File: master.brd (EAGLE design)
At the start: 27.3 x 34.3 mm, 9 parts

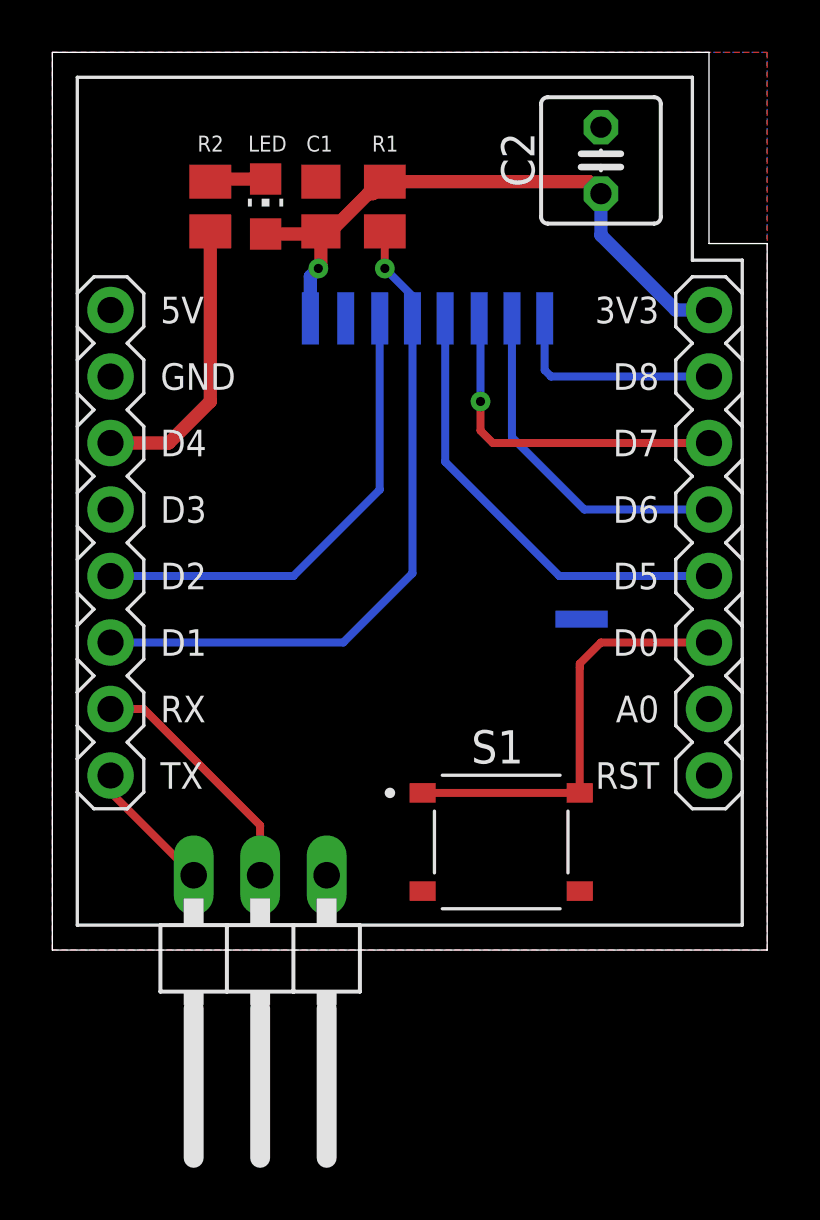
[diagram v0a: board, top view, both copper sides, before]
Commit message: poprawione polaczenia, usunieta masa pod antena,
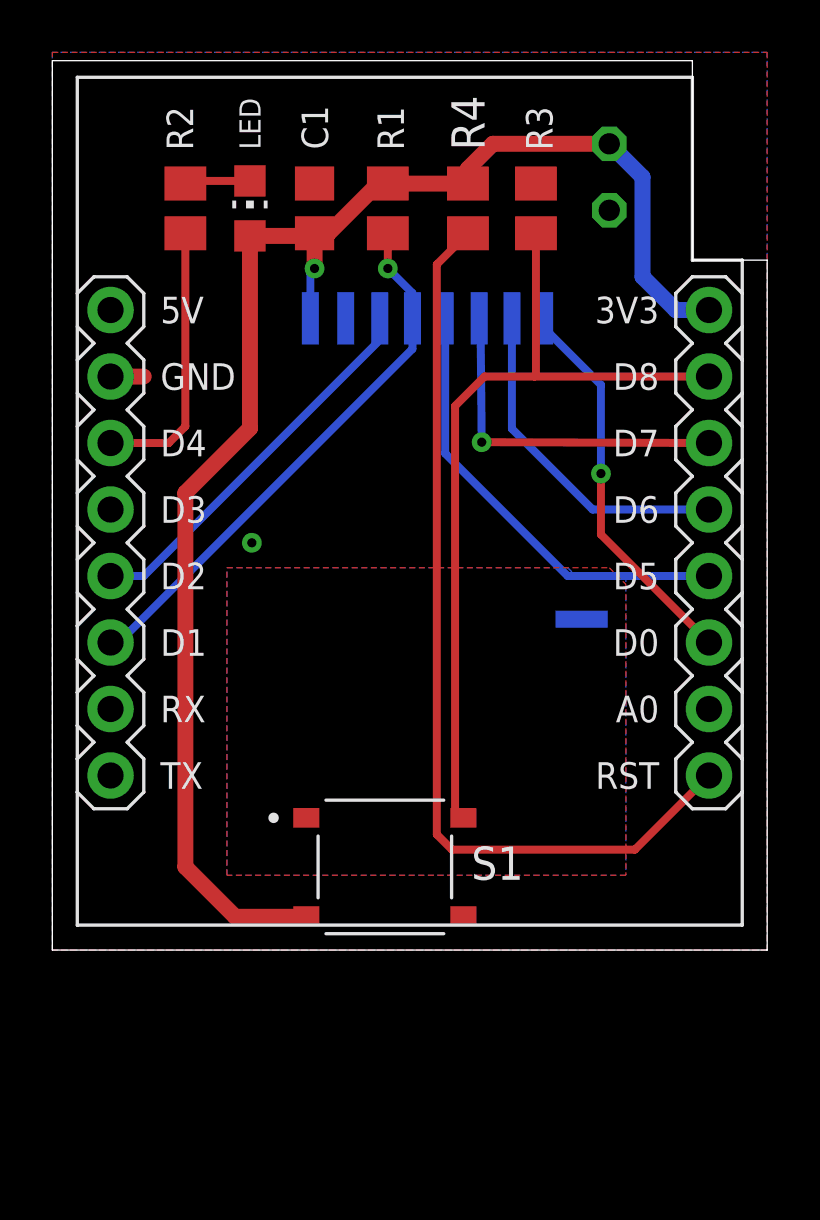
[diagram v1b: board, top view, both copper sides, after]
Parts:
- removed JP2: (no value), pinhead:1X03/90
- added R3: 47k, rcl:M0805
- added R4: 100k, rcl:M0805
- moved S1 4.55 mm to (12.7, 3.17)
- moved R2 0.96 mm to (5.08, 28.3)
- moved C2 0.71 mm to (21.3, 29.5), flipped to the bottom, turned to 270 degrees
- moved LED 0.60 mm to (7.55, 28.3)
- moved C1 0.25 mm to (10.0, 28.3)
- moved R1 0.14 mm to (12.8, 28.3)
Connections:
- removed net RX: JP2.2, U$2.JP2.2
- removed net TX: JP2.3, U$2.JP2.1
- new net RST: R4.2, U$2.JP1.1
- net +3V3: now also R4.1, S1.C, S1.D
- net BUTTON: now also R3.1, U$2.JP1.7; no longer U$2.JP1.3
- net GND: now also R3.2; no longer JP2.1, S1.C, S1.D
- net INTERRUPT: now also U$2.JP1.3; no longer U$2.JP1.7
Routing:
- net RST: track 0.00 -> 35.3 mm
- net +3V3: track 24.8 -> 58.1 mm
- net BUTTON: track 16.2 -> 31.7 mm
- net RX: track 9.46 -> 0.00 mm
- net INTERRUPT: track 8.36 -> 15.0 mm, vias 0 -> 1
- net CSN: track 26.1 -> 21.0 mm
- net TX: track 5.13 -> 0.00 mm
- net CE: track 18.2 -> 14.8 mm
- net GND: track 0.00 -> 1.27 mm, vias 0 -> 1
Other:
- board size 27.3 x 34.3 mm -> 27.3 x 34 mm
- board text removed: "C1"
- board text removed: "C2"
- board text removed: "LED"
- board text removed: "R1"
- board text removed: "R2"
- board text removed: "S1"

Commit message: dodanei warstwy opisowej do panelizacji
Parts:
- moved S1 7.30 mm to (20.0, 3.17)
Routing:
- net +3V3: track 58.1 -> 71.4 mm
- net BUTTON: track 31.7 -> 39.2 mm
- net RST: track 35.3 -> 36.0 mm
- net MOSI: track 13.4 -> 13.2 mm, vias 1 -> 0
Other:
- board text added: "C1"
- board text added: "C2"
- board text added: "LED"
- board text added: "R1"
- board text added: "R2"
- board text added: "R3"
- board text added: "R4"
- board text added: "S1"
- board text added: "by Dominik Nowocień v1.1"
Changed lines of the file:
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@@
 <drawing>
 <settings>
-<setting alwaysvectorfont="no"/>
+<setting alwaysvectorfont="yes"/>
 <setting verticaltext="up"/>
 </settings>
@@
 <layer number="97" name="Info" color="7" fill="1" visible="no" active="no"/>
 <layer number="98" name="Guide" color="6" fill="1" visible="no" active="no"/>
-<layer number="101" name="Hidden" color="15" fill="1" visible="yes" active="yes"/>
-<layer number="102" name="Changes" color="12" fill="1" visible="yes" active="yes"/>
-<layer number="125" name="_tNames" color="7" fill="1" visible="no" active="yes"/>
+<layer number="100" name="opis_dol" color="7" fill="1" visible="yes" active="yes"/>
+<layer number="101" name="opis_gora" color="7" fill="1" visible="no" active="yes"/>
+<layer number="125" name="_tNames" color="14" fill="1" visible="yes" active="yes"/>
+<layer number="126" name="_bNames" color="5" fill="1" visible="yes" active="yes"/>
 </layers>
 <board>
@@
 <wire x1="0" y1="0" x2="27.305" y2="0" width="0" layer="20"/>
 <text x="6.6675" y="20.6375" size="1.4224" layer="22" rot="MR270">NRF24L01+</text>
+<text x="13.75" y="3.135" size="1.27" layer="100" rot="SR180" align="center">by Dominik Nowocień v1.1</text>
+<text x="10.534115625" y="30.582540625" size="1.016" layer="125" rot="R90">C1</text>
+<text x="18.415" y="30.226" size="1.27" layer="126" ratio="10" rot="MR270">C2</text>
+<text x="7.9558125" y="30.582540625" size="0.8128" layer="125" rot="R90">LED</text>
+<text x="13.42991875" y="30.551653125" size="1.016" layer="125" rot="R90">R1</text>
+<text x="5.377509375" y="30.551653125" size="1.016" layer="125" rot="R90">R2</text>
+<text x="19.10745625" y="30.551653125" size="1.016" layer="125" rot="R90">R3</text>
+<text x="16.51" y="30.551653125" size="1.27" layer="125" rot="R90">R4</text>
+<text x="23.305009375" y="2.68249375" size="1.27" layer="125">S1</text>
 </plain>
 <attributes>
@@
 <attribute name="VALUE" x="7.62" y="27.05915" size="1.27" layer="27" rot="R90"/>
 </element>
-<element name="S1" library="Modules" package="SW_TS-1187A-B-A-B" package3d_urn="urn:adsk.eagle:package:24754950/2" value="TS-1187A-B-A-B" x="12.7" y="3.175" smashed="yes">
-<attribute name="NAME" x="16.0025" y="2.6825" size="1.27" layer="25"/>
+<element name="S1" library="Modules" package="SW_TS-1187A-B-A-B" package3d_urn="urn:adsk.eagle:package:24754950/2" value="TS-1187A-B-A-B" x="20.0025" y="3.175" smashed="yes">
+<attribute name="NAME" x="23.305" y="2.6825" size="1.27" layer="25"/>
 </element>
 <element name="R3" library="rcl" library_urn="urn:adsk.eagle:library:334" package="M0805" package3d_urn="urn:adsk.eagle:package:23556/2" value="47k" x="18.47245" y="28.32915" smashed="yes" rot="R90">
@@
 <wire x1="5.08" y1="17.4625" x2="5.08" y2="3.175" width="0.6096" layer="1"/>
 <wire x1="5.08" y1="3.175" x2="6.985" y2="1.27" width="0.6096" layer="1"/>
-<wire x1="6.985" y1="1.27" x2="9.67" y2="1.27" width="0.6096" layer="1"/>
-<wire x1="9.67" y1="1.27" x2="9.7" y2="1.3" width="0.3048" layer="1"/>
-<wire x1="10.014875" y1="26.035" x2="9.855" y2="25.875125" width="0.3048" layer="16"/>
-<wire x1="9.855" y1="25.875125" x2="9.855" y2="24.13" width="0.3048" layer="16"/>
-<wire x1="9.7" y1="1.3" x2="15.7" y2="1.3" width="0" layer="19" extent="1-1"/>
+<wire x1="16.9725" y1="1.27" x2="6.985" y2="1.27" width="0.6096" layer="1"/>
+<wire x1="9.855" y1="24.13" x2="9.855" y2="25.875125" width="0.5" layer="16"/>
+<wire x1="9.855" y1="25.875125" x2="10.014875" y2="26.035" width="0.5" layer="16"/>
+<wire x1="17.0025" y1="1.3" x2="23.0025" y2="1.3" width="0.5" layer="1"/>
+<wire x1="17.0025" y1="1.3" x2="16.9725" y2="1.27" width="0.5" layer="1"/>
 </signal>
 <signal name="GND" class="1">
@@
 <signal name="MOSI">
 <contactref element="U$2" pad="JP1.6"/>
-<via x="16.4" y="19.4" extent="1-16" drill="0.35"/>
-<wire x1="16.4" y1="19.4" x2="16.3546" y2="24.0804" width="0.3048" layer="16"/>
-<wire x1="16.3546" y1="24.0804" x2="16.305" y2="24.13" width="0.3048" layer="16"/>
+<wire x1="16.305" y1="24.13" x2="16.41465" y2="24.23965" width="0.3048" layer="16"/>
 <contactref element="NRF24" pad="6"/>
-<wire x1="25.0825" y1="19.3675" x2="16.4" y2="19.4" width="0.3048" layer="1"/>
+<wire x1="16.305" y1="24.13" x2="16.305" y2="25.195" width="0.5" layer="16"/>
+<wire x1="16.305" y1="25.195" x2="16.8275" y2="25.7175" width="0.5" layer="16"/>
+<wire x1="16.8275" y1="25.7175" x2="19.3675" y2="25.7175" width="0.5" layer="16"/>
+<wire x1="23.495" y1="21.59" x2="23.495" y2="20.955" width="0.5" layer="16"/>
+<wire x1="23.495" y1="20.955" x2="25.0825" y2="19.3675" width="0.5" layer="16"/>
+<wire x1="19.3675" y1="25.7175" x2="23.495" y2="21.59" width="0.5" layer="16"/>
 </signal>
 <signal name="CSN">
@@
 <contactref element="U$2" pad="JP1.7"/>
 <wire x1="15.3825" y1="20.78" x2="15.3825" y2="5.05" width="0.3048" layer="1"/>
-<wire x1="15.7" y1="5.05" x2="15.3825" y2="5.05" width="0.3048" layer="1"/>
+<wire x1="23.0025" y1="5.05" x2="17.145" y2="5.05" width="0.3048" layer="1"/>
+<wire x1="17.145" y1="5.05" x2="15.3825" y2="5.05" width="0.3048" layer="1"/>
 <wire x1="25.0825" y1="21.9075" x2="18.415" y2="21.9075" width="0.3048" layer="1"/>
 <contactref element="S1" pad="B"/>
@@
 <wire x1="15.3825" y1="20.78" x2="16.51" y2="21.9075" width="0.3048" layer="1"/>
 <wire x1="16.51" y1="21.9075" x2="18.415" y2="21.9075" width="0.3048" layer="1"/>
-<wire x1="9.7" y1="5.05" x2="15.7" y2="5.05" width="0" layer="19" extent="1-1"/>
+<wire x1="17.0025" y1="5.05" x2="17.145" y2="5.05" width="0.1524" layer="1"/>
 </signal>
 <signal name="INTERRUPT">
@@
 <wire x1="14.6852" y1="26.1893625" x2="14.6852" y2="4.415" width="0.3048" layer="1"/>
 <wire x1="15.2651" y1="3.8351" x2="14.6852" y2="4.415" width="0.3048" layer="1"/>
-<wire x1="25.0825" y1="6.6675" x2="22.2501" y2="3.8351" width="0.3048" layer="1"/>
-<wire x1="22.2501" y1="3.8351" x2="15.2651" y2="3.8351" width="0.3048" layer="1"/>
+<wire x1="25.0825" y1="6.6675" x2="25.0825" y2="5.3975" width="0.3048" layer="1"/>
+<wire x1="25.0825" y1="5.3975" x2="23.5201" y2="3.8351" width="0.3048" layer="1"/>
+<wire x1="23.5201" y1="3.8351" x2="15.2651" y2="3.8351" width="0.3048" layer="1"/>
 </signal>
 </signals>

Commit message: drobne poprawki
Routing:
- net RST: track 36.0 -> 50.3 mm
- net BUTTON: track 39.2 -> 27.1 mm
- net SCK: track 17.2 -> 14.9 mm
- net MISO: track 13.0 -> 11.5 mm
- net GND: vias 1 -> 2
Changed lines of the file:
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@@
 </layers>
 <board>
-<fusionsync huburn="a.YnVzaW5lc3M6c3R1ZGVudDQ4Njkw" projecturn="a.YnVzaW5lc3M6c3R1ZGVudDQ4NjkwI0QyMDIwMTEwOTM1MTQzNTM4MQ" f3durn="urn:adsk.wipprod:dm.lineage:U4Mw_bNETOOnVXnWI0y87Q" pcbguid="" lastpulledtime="" lastsyncedchangeguid="" latestrevisionid="d24e285d-8679-4091-b8af-5643a4074593" lastsyncedrevisionid="d24e285d-8679-4091-b8af-5643a4074593" lastboardhashguid="a275b44c-f568-7217-ba50-b1bd45fb6022" lastpushedtime="2020-12-21T23:49:28Z" linktopcb3d="true"/>
+<fusionsync huburn="a.YnVzaW5lc3M6c3R1ZGVudDQ4Njkw" projecturn="a.YnVzaW5lc3M6c3R1ZGVudDQ4NjkwI0QyMDIwMTEwOTM1MTQzNTM4MQ" f3durn="urn:adsk.wipprod:dm.lineage:U4Mw_bNETOOnVXnWI0y87Q" pcbguid="" lastpulledtime="" lastsyncedchangeguid="" latestrevisionid="adf31d11-2971-490c-9e2a-feead3d7f8aa" lastsyncedrevisionid="adf31d11-2971-490c-9e2a-feead3d7f8aa" lastboardhashguid="4a1d11f1-682a-e53e-9940-e431d41f0d06" lastpushedtime="2020-12-31T12:38:42Z" linktopcb3d="true"/>
 <plain>
 <wire x1="27.305" y1="26.3525" x2="24.4475" y2="26.3525" width="0" layer="20"/>
@@
 <contactref element="LED" pad="A"/>
 <contactref element="U$2" pad="JP1.8"/>
-<wire x1="10.014875" y1="27.37915" x2="10.014875" y2="26.035" width="0.6096" layer="1"/>
-<via x="10.014875" y="26.035" extent="1-16" drill="0.35"/>
+<wire x1="10.014875" y1="27.37915" x2="10.014875" y2="26" width="0.6096" layer="1"/>
+<via x="10.014875" y="26" extent="1-16" drill="0.35"/>
 <wire x1="9.88615" y1="27.3508" x2="9.8145" y2="27.27915" width="0.6096" layer="1"/>
 <wire x1="9.8145" y1="27.27915" x2="7.5474375" y2="27.27915" width="0.6096" layer="1"/>
@@
 <wire x1="16.9725" y1="1.27" x2="6.985" y2="1.27" width="0.6096" layer="1"/>
 <wire x1="9.855" y1="24.13" x2="9.855" y2="25.875125" width="0.5" layer="16"/>
-<wire x1="9.855" y1="25.875125" x2="10.014875" y2="26.035" width="0.5" layer="16"/>
+<wire x1="9.855" y1="25.875125" x2="10.014875" y2="26" width="0.5" layer="16"/>
 <wire x1="17.0025" y1="1.3" x2="23.0025" y2="1.3" width="0.5" layer="1"/>
 <wire x1="17.0025" y1="1.3" x2="16.9725" y2="1.27" width="0.5" layer="1"/>
@@
 </polygon>
 <polygon width="0.3048" layer="1" pour="cutout">
-<vertex x="6.6675" y="14.605"/>
+<vertex x="6.35" y="14.605"/>
 <vertex x="21.2725" y="14.605"/>
 <vertex x="21.9075" y="13.97"/>
 <vertex x="21.9075" y="2.8575"/>
-<vertex x="6.6675" y="2.8575"/>
+<vertex x="6.35" y="2.8575"/>
 </polygon>
 <polygon width="0.3048" layer="16" pour="cutout">
 <vertex x="6.6675" y="14.605"/>
-<vertex x="19.685" y="14.605"/>
-<vertex x="20.0025" y="14.2875"/>
-<vertex x="21.9075" y="14.2875"/>
+<vertex x="21.9075" y="14.605"/>
 <vertex x="21.9075" y="2.8575"/>
 <vertex x="6.6675" y="2.8575"/>
@@
 <wire x1="2.2225" y1="21.9075" x2="3.4925" y2="21.9075" width="0.6096" layer="1"/>
 <via x="7.62" y="15.5575" extent="1-16" drill="0.35"/>
+<via x="8.5725" y="25.7175" extent="1-16" drill="0.35"/>
 </signal>
 <signal name="SCK">
 <contactref element="U$2" pad="JP1.4"/>
-<wire x1="25.0825" y1="14.2875" x2="19.685" y2="14.2875" width="0.3048" layer="16"/>
-<wire x1="15.005" y1="18.9675" x2="15.005" y2="24.13" width="0.3048" layer="16"/>
-<wire x1="19.685" y1="14.2875" x2="15.005" y2="18.9675" width="0.3048" layer="16"/>
+<wire x1="25.0825" y1="14.2875" x2="23.495" y2="14.2875" width="0.3048" layer="16"/>
+<wire x1="15.005" y1="22.7775" x2="15.005" y2="24.13" width="0.3048" layer="16"/>
+<wire x1="23.495" y1="14.2875" x2="15.005" y2="22.7775" width="0.3048" layer="16"/>
 <contactref element="NRF24" pad="5"/>
 </signal>
 <signal name="MISO">
 <contactref element="U$2" pad="JP1.5"/>
-<wire x1="25.0825" y1="16.8275" x2="20.6375" y2="16.8275" width="0.3048" layer="16"/>
-<wire x1="20.6375" y1="16.8275" x2="17.555" y2="19.91" width="0.3048" layer="16"/>
-<wire x1="17.555" y1="19.91" x2="17.555" y2="24.13" width="0.3048" layer="16"/>
+<wire x1="25.0825" y1="16.8275" x2="23.1775" y2="16.8275" width="0.3048" layer="16"/>
+<wire x1="23.1775" y1="16.8275" x2="17.555" y2="22.45" width="0.3048" layer="16"/>
+<wire x1="17.555" y1="22.45" x2="17.555" y2="24.13" width="0.3048" layer="16"/>
 <contactref element="NRF24" pad="7"/>
 </signal>
@@
 <wire x1="16.305" y1="24.13" x2="16.41465" y2="24.23965" width="0.3048" layer="16"/>
 <contactref element="NRF24" pad="6"/>
-<wire x1="16.305" y1="24.13" x2="16.305" y2="25.195" width="0.5" layer="16"/>
-<wire x1="16.305" y1="25.195" x2="16.8275" y2="25.7175" width="0.5" layer="16"/>
-<wire x1="16.8275" y1="25.7175" x2="19.3675" y2="25.7175" width="0.5" layer="16"/>
-<wire x1="23.495" y1="21.59" x2="23.495" y2="20.955" width="0.5" layer="16"/>
-<wire x1="23.495" y1="20.955" x2="25.0825" y2="19.3675" width="0.5" layer="16"/>
-<wire x1="19.3675" y1="25.7175" x2="23.495" y2="21.59" width="0.5" layer="16"/>
+<wire x1="16.305" y1="24.13" x2="16.305" y2="25.195" width="0.3048" layer="16"/>
+<wire x1="16.305" y1="25.195" x2="16.8275" y2="25.7175" width="0.3048" layer="16"/>
+<wire x1="16.8275" y1="25.7175" x2="19.3675" y2="25.7175" width="0.3048" layer="16"/>
+<wire x1="22.5425" y1="22.5425" x2="22.5425" y2="21.9075" width="0.3048" layer="16"/>
+<wire x1="22.5425" y1="21.9075" x2="25.0825" y2="19.3675" width="0.3048" layer="16"/>
+<wire x1="19.3675" y1="25.7175" x2="22.5425" y2="22.5425" width="0.3048" layer="16"/>
 </signal>
 <signal name="CSN">
@@
 <wire x1="13.755" y1="22.9625" x2="2.54" y2="11.7475" width="0.3048" layer="16"/>
 <wire x1="2.2225" y1="11.7475" x2="2.54" y2="11.7475" width="0.3048" layer="16"/>
-<wire x1="12.8149125" y1="27.37915" x2="12.8149125" y2="26.035" width="0.3048" layer="1"/>
-<via x="12.8149125" y="26.035" extent="1-16" drill="0.35"/>
+<wire x1="12.8149125" y1="27.37915" x2="12.8149125" y2="26" width="0.3048" layer="1"/>
+<via x="12.8149125" y="26" extent="1-16" drill="0.35"/>
 <contactref element="NRF24" pad="4"/>
-<wire x1="12.8149125" y1="26.035" x2="13.755" y2="25.0949125" width="0.3048" layer="16"/>
+<wire x1="12.8149125" y1="26" x2="13.755" y2="25.0949125" width="0.3048" layer="16"/>
 <wire x1="13.755" y1="25.0949125" x2="13.755" y2="24.13" width="0.3048" layer="16"/>
 </signal>
@@
 <signal name="BUTTON">
 <contactref element="U$2" pad="JP1.7"/>
-<wire x1="15.3825" y1="20.78" x2="15.3825" y2="5.05" width="0.3048" layer="1"/>
-<wire x1="23.0025" y1="5.05" x2="17.145" y2="5.05" width="0.3048" layer="1"/>
-<wire x1="17.145" y1="5.05" x2="15.3825" y2="5.05" width="0.3048" layer="1"/>
-<wire x1="25.0825" y1="21.9075" x2="18.415" y2="21.9075" width="0.3048" layer="1"/>
+<wire x1="25.0825" y1="21.9075" x2="22.3675" y2="21.9075" width="0.3048" layer="1"/>
 <contactref element="S1" pad="B"/>
 <contactref element="S1" pad="A"/>
 <contactref element="R3" pad="1"/>
-<wire x1="18.47245" y1="27.37915" x2="18.47245" y2="21.96495" width="0.3048" layer="1"/>
-<wire x1="18.47245" y1="21.96495" x2="18.415" y2="21.9075" width="0.3048" layer="1"/>
-<wire x1="15.3825" y1="20.78" x2="16.51" y2="21.9075" width="0.3048" layer="1"/>
-<wire x1="16.51" y1="21.9075" x2="18.415" y2="21.9075" width="0.3048" layer="1"/>
+<wire x1="18.47245" y1="27.37915" x2="18.47245" y2="25.7175" width="0.3048" layer="1"/>
 <wire x1="17.0025" y1="5.05" x2="17.145" y2="5.05" width="0.1524" layer="1"/>
+<wire x1="22.3675" y1="21.9075" x2="22.28245" y2="21.9075" width="0.3048" layer="1"/>
+<wire x1="22.28245" y1="21.9075" x2="18.47245" y2="25.7175" width="0.3048" layer="1"/>
+<wire x1="22.3675" y1="5.685" x2="23.0025" y2="5.05" width="0.3048" layer="1"/>
+<wire x1="22.3675" y1="21.9075" x2="22.3675" y2="5.685" width="0.3048" layer="1"/>
+<wire x1="17.145" y1="5.05" x2="23.0025" y2="5.05" width="0" layer="19" extent="1-1"/>
 </signal>
 <signal name="INTERRUPT">
@@
 <contactref element="NRF24" pad="8"/>
 <contactref element="U$2" pad="JP1.3"/>
-<wire x1="25.0825" y1="11.7475" x2="20.955" y2="15.875" width="0.3048" layer="1"/>
-<wire x1="20.955" y1="15.875" x2="20.955" y2="18.2" width="0.3048" layer="1"/>
-<via x="20.955" y="18.2" extent="1-16" drill="0.35"/>
-<wire x1="20.955" y1="18.2" x2="20.955" y2="21.59" width="0.3048" layer="16"/>
-<wire x1="20.955" y1="21.59" x2="18.805" y2="23.74" width="0.3048" layer="16"/>
+<wire x1="25.0825" y1="11.7475" x2="23.495" y2="13.335" width="0.3048" layer="1"/>
+<wire x1="23.495" y1="13.335" x2="23.495" y2="18.2" width="0.3048" layer="1"/>
+<via x="23.495" y="18.2" extent="1-16" drill="0.35"/>
+<wire x1="23.495" y1="18.2" x2="23.495" y2="19.05" width="0.3048" layer="16"/>
+<wire x1="23.495" y1="19.05" x2="18.805" y2="23.74" width="0.3048" layer="16"/>
 </signal>
 <signal name="LED1">
@@
 <contactref element="U$2" pad="JP1.1"/>
 <contactref element="R4" pad="2"/>
-<wire x1="15.8749875" y1="27.37915" x2="14.6852" y2="26.1893625" width="0.3048" layer="1"/>
-<wire x1="14.6852" y1="26.1893625" x2="14.6852" y2="4.415" width="0.3048" layer="1"/>
-<wire x1="15.2651" y1="3.8351" x2="14.6852" y2="4.415" width="0.3048" layer="1"/>
+<wire x1="15.8749875" y1="27.37915" x2="5.7952" y2="17.2993625" width="0.3048" layer="1"/>
+<wire x1="5.7952" y1="17.2993625" x2="5.7952" y2="3.78" width="0.3048" layer="1"/>
+<wire x1="7.3276" y1="2.2476" x2="5.7952" y2="3.78" width="0.3048" layer="1"/>
 <wire x1="25.0825" y1="6.6675" x2="25.0825" y2="5.3975" width="0.3048" layer="1"/>
-<wire x1="25.0825" y1="5.3975" x2="23.5201" y2="3.8351" width="0.3048" layer="1"/>
-<wire x1="23.5201" y1="3.8351" x2="15.2651" y2="3.8351" width="0.3048" layer="1"/>
+<wire x1="25.0825" y1="5.3975" x2="21.9326" y2="2.2476" width="0.3048" layer="1"/>
+<wire x1="21.9326" y1="2.2476" x2="7.3276" y2="2.2476" width="0.3048" layer="1"/>
 </signal>
 </signals>
